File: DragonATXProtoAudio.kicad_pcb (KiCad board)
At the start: 2 copper layers, 159.4 x 50.4 mm, 17 parts, among them IC1 74LS138, IC2 74LS08, J3 Audio Left, J4 Audio Right, J8 Stereo

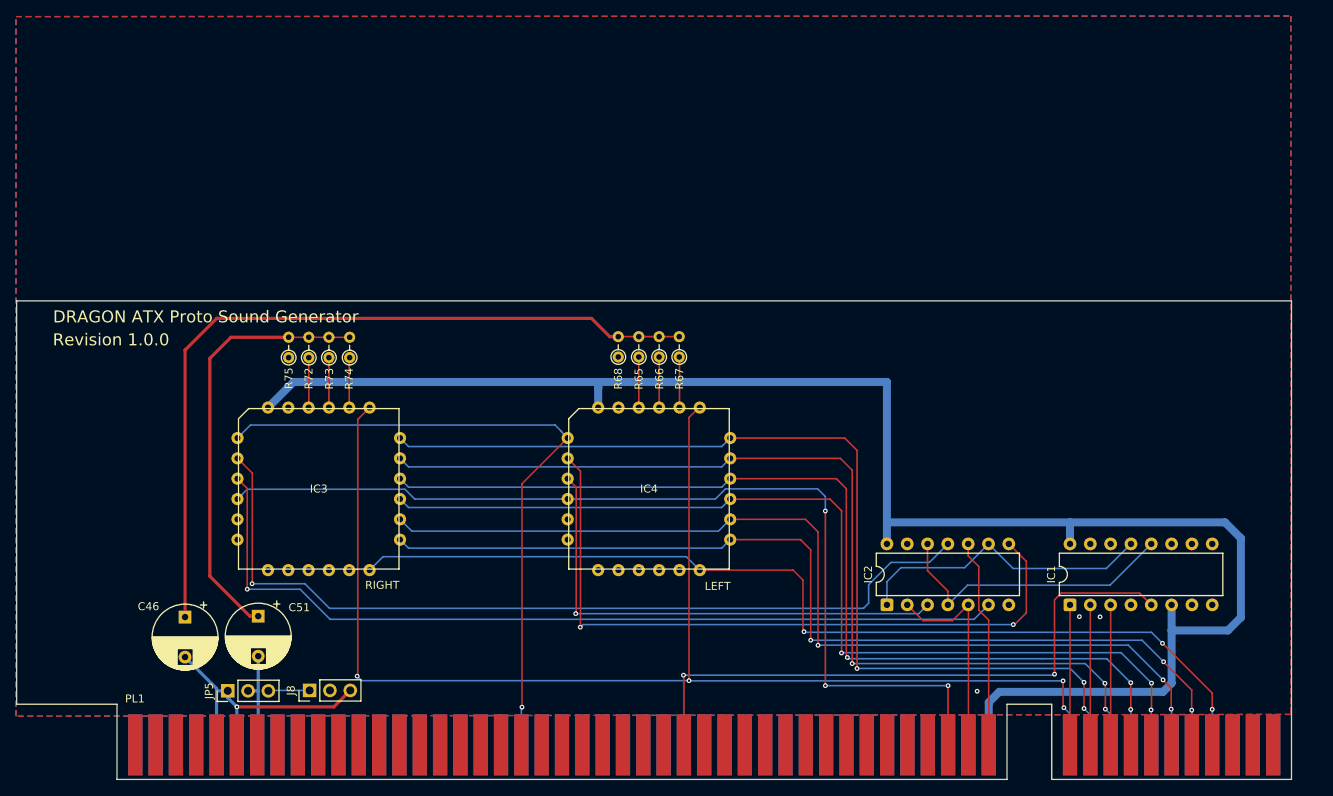
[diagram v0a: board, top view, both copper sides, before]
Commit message: upgrade card edge spec
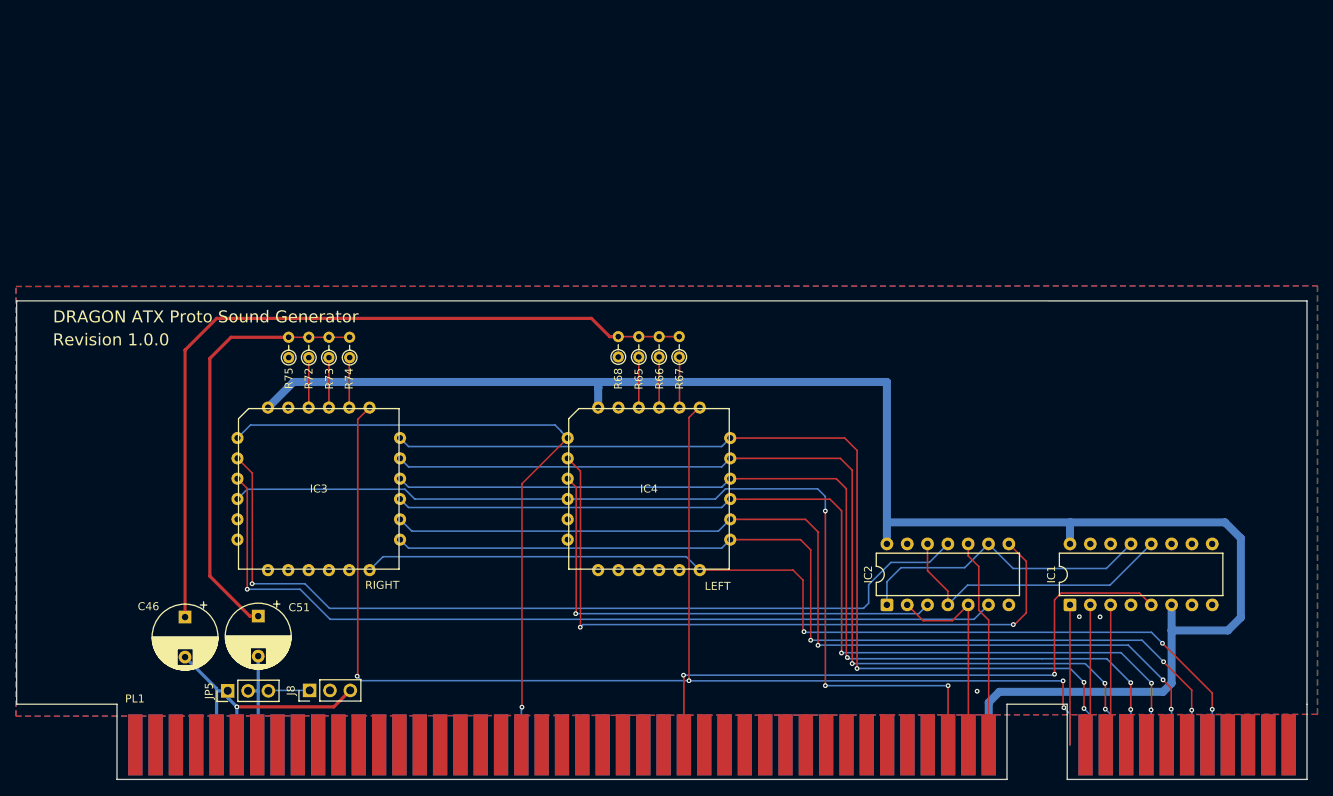
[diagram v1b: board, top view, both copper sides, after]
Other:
- board size 159.4 x 50.4 mm -> 161.3 x 50.4 mm
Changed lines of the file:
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@@
 		(fp_line
 			(start 35.179 -7.874)
-			(end 40.767 -7.874)
+			(end 42.707 -7.874)
 			(stroke
 				(width 0.05)
@@
 		)
 		(fp_line
-			(start 40.767 -7.874)
-			(end 40.767 1.524)
+			(start 42.707 -7.874)
+			(end 42.707 1.524)
 			(stroke
 				(width 0.05)
-				(type default)
+				(type solid)
 			)
 			(layer "Edge.Cuts")
 		)
 		(fp_line
-			(start 40.767 1.524)
-			(end 70.739 1.524)
+			(start 42.707 1.524)
+			(end 72.679 1.524)
 			(stroke
 				(width 0.05)
@@
 		)
 		(fp_line
-			(start 70.739 1.524)
-			(end 70.739 -7.874)
+			(start 72.679 1.524)
+			(end 72.679 -7.874)
 			(stroke
 				(width 0.05)
-				(type default)
+				(type solid)
 			)
 			(layer "Edge.Cuts")
@@
 		)
 		(pad "c1" connect rect
-			(at 43.053 -2.794)
+			(at 44.993 -2.794)
 			(size 1.78 7.62)
 			(layers "F.Cu" "F.Mask")
@@
 		)
 		(pad "c2" connect rect
-			(at 45.593 -2.794)
+			(at 47.533 -2.794)
 			(size 1.78 7.62)
 			(layers "F.Cu" "F.Mask")
@@
 		)
 		(pad "c3" connect rect
-			(at 48.141266 -2.805199)
+			(at 50.081266 -2.805199)
 			(size 1.78 7.62)
 			(layers "F.Cu" "F.Mask")
@@
 		)
 		(pad "c4" connect rect
-			(at 50.673 -2.794)
+			(at 52.613 -2.794)
 			(size 1.78 7.62)
 			(layers "F.Cu" "F.Mask")
@@
 		)
 		(pad "c5" connect rect
-			(at 53.213 -2.794)
+			(at 55.153 -2.794)
 			(size 1.78 7.62)
 			(layers "F.Cu" "F.Mask")
@@
 		)
 		(pad "c6" connect rect
-			(at 55.753 -2.794)
+			(at 57.693 -2.794)
 			(size 1.78 7.62)
 			(layers "F.Cu" "F.Mask")
@@
 		)
 		(pad "c7" connect rect
-			(at 58.293 -2.794)
+			(at 60.233 -2.794)
 			(size 1.78 7.62)
 			(layers "F.Cu" "F.Mask")
@@
 		)
 		(pad "c8" connect rect
-			(at 60.833 -2.794)
+			(at 62.773 -2.794)
 			(size 1.78 7.62)
 			(layers "F.Cu" "F.Mask")
@@
 		)
 		(pad "c9" connect rect
-			(at 63.373 -2.794)
+			(at 65.313 -2.794)
 			(size 1.78 7.62)
 			(layers "F.Cu" "F.Mask")
@@
 		)
 		(pad "c10" connect rect
-			(at 65.913 -2.794)
+			(at 67.853 -2.794)
 			(size 1.78 7.62)
 			(layers "F.Cu" "F.Mask")
@@
 		)
 		(pad "c11" connect rect
-			(at 68.453 -2.794)
+			(at 70.393 -2.794)
 			(size 1.78 7.62)
 			(layers "F.Cu" "F.Mask")
@@
 		)
 		(pad "d1" connect rect
-			(at 43.053 -2.794)
+			(at 44.9834 -2.794)
 			(size 1.78 7.62)
 			(layers "B.Cu" "B.Mask")
@@
 		)
 		(pad "d2" connect rect
-			(at 45.593 -2.794)
+			(at 47.5234 -2.794)
 			(size 1.78 7.62)
 			(layers "B.Cu" "B.Mask")
@@
 		)
 		(pad "d3" connect rect
-			(at 48.141266 -2.782801)
+			(at 50.071666 -2.782801)
 			(size 1.78 7.62)
 			(layers "B.Cu" "B.Mask")
@@
 		)
 		(pad "d4" connect rect
-			(at 50.673 -2.794)
+			(at 52.6034 -2.794)
 			(size 1.78 7.62)
 			(layers "B.Cu" "B.Mask")
@@
 		)
 		(pad "d5" connect rect
-			(at 53.213 -2.794)
+			(at 55.1434 -2.794)
 			(size 1.78 7.62)
 			(layers "B.Cu" "B.Mask")
@@
 		)
 		(pad "d6" connect rect
-			(at 55.753 -2.794)
+			(at 57.6834 -2.794)
 			(size 1.78 7.62)
 			(layers "B.Cu" "B.Mask")
@@
 		)
 		(pad "d7" connect rect
-			(at 58.293 -2.794)
+			(at 60.2234 -2.794)
 			(size 1.78 7.62)
 			(layers "B.Cu" "B.Mask")
@@
 		)
 		(pad "d8" connect rect
-			(at 60.833 -2.794)
+			(at 62.7634 -2.794)
 			(size 1.78 7.62)
 			(layers "B.Cu" "B.Mask")
@@
 		)
 		(pad "d9" connect rect
-			(at 63.373 -2.794)
+			(at 65.3034 -2.794)
 			(size 1.78 7.62)
 			(layers "B.Cu" "B.Mask")
@@
 		)
 		(pad "d10" connect rect
-			(at 65.913 -2.794)
+			(at 67.8434 -2.794)
 			(size 1.78 7.62)
 			(layers "B.Cu" "B.Mask")
@@
 		)
 		(pad "d11" connect rect
-			(at 68.453 -2.794)
+			(at 70.3834 -2.794)
 			(size 1.78 7.62)
 			(layers "B.Cu" "B.Mask")
@@
 	(gr_line
 		(start 52.0766 93.3704)
-		(end 211.4296 93.3704)
+		(end 213.369211 93.372868)
 		(stroke
 			(width 0.05)
@@
 	)
 	(gr_line
-		(start 211.4296 143.7894)
-		(end 211.4296 93.3704)
+		(start 213.369211 143.791868)
+		(end 213.369211 93.372868)
 		(stroke
 			(width 0.05)
@@
 		(polygon
 			(pts
-				(xy 51.9938 57.8358) (xy 211.3534 57.7596) (xy 211.3534 145.0594) (xy 51.9938 145.288)
+				(xy 51.9938 91.568999) (xy 214.6808 91.491208) (xy 214.6808 145.054626) (xy 51.9938 145.288)
 			)
 		)

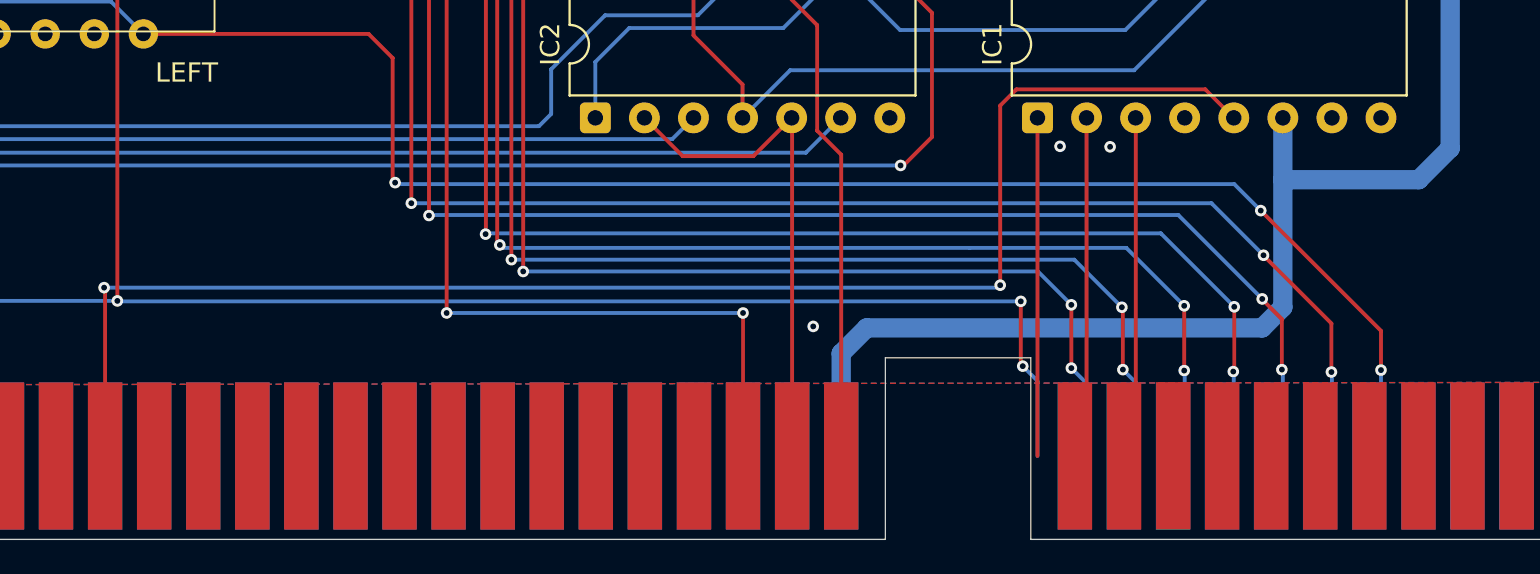
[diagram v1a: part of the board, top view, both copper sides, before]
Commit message: fix routing for new card edge spec
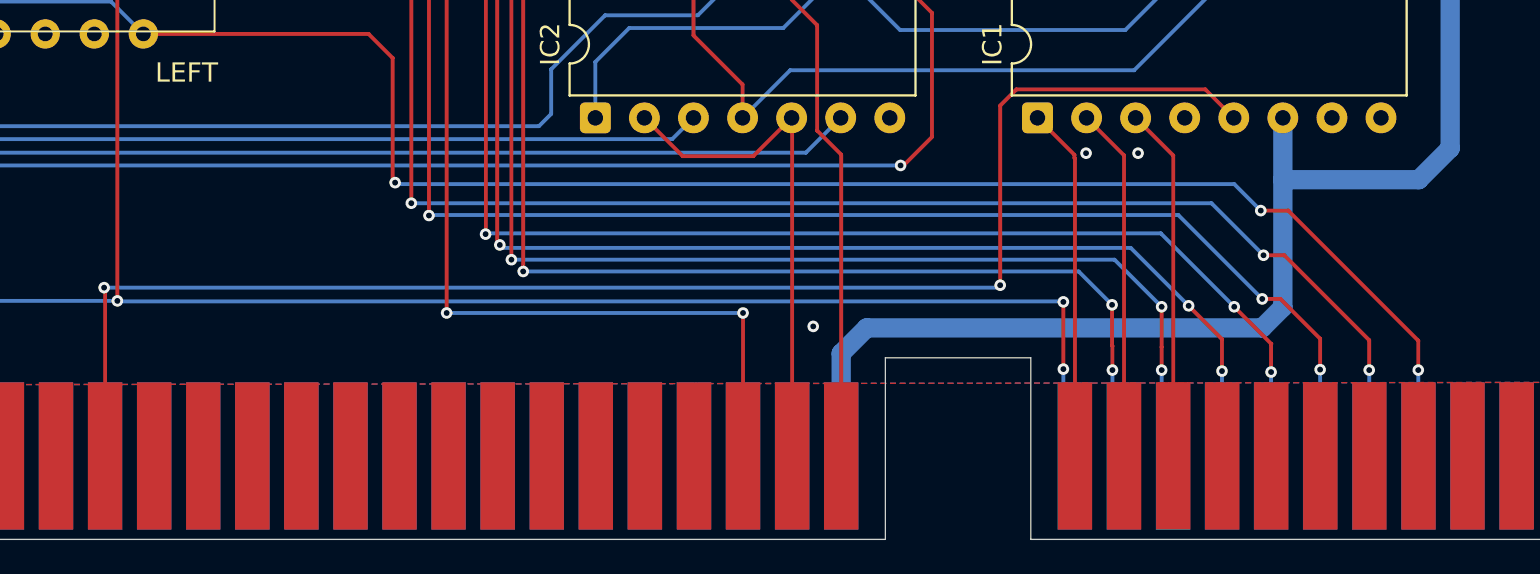
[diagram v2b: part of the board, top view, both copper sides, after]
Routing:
- net /D0: track 165.8 -> 167.9 mm
- net /D1: track 123.1 -> 125.2 mm
- net /D2: track 122.8 -> 124.8 mm
- net /D7: track 123.3 -> 124.9 mm
- net /D6: track 120.9 -> 122.3 mm
- net /D5: track 121.8 -> 123.2 mm
- net /D3: track 122.8 -> 123.8 mm
- net /A2: track 17.5 -> 18.3 mm
- net /A4: track 17.5 -> 18.3 mm
- net /A3: track 17.5 -> 18.3 mm
- net /D4: track 122.6 -> 123.3 mm
